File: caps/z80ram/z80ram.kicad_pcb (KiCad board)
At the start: 4 copper layers, 85 x 56 mm, 19 parts, among them J10 PORTG, J2 PORTA, J3 PORTB, J5 PORTD, J6 PORTE, J7 PORTF, U1 74HCT257, U2 AS6C4008-55PCN, U3 74HCT574, U4 Z80CPU

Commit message: OCD tweaks
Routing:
- net /PA6: track 90.7 -> 87.6 mm
- net /PD2: track 69.2 -> 66.7 mm
- net /PD6: track 62.3 -> 60.9 mm
- net /PD4: track 65.3 -> 64.1 mm
- net /PE2: track 131.9 -> 133.1 mm
- net /PB1: track 35.1 -> 36.0 mm
- net /PE0: track 111.4 -> 112.0 mm
- net /PD5: track 57.9 -> 57.2 mm
- net GND: vias 81 -> 82

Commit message: Final (?!) tweaks
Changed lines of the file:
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@@
 	)
 	(segment
-		(start 182.481637 110.043082)
-		(end 182.481637 109.15472)
+		(start 182.25 110.274719)
+		(end 182.25 109.386357)
 		(width 0.25)
 		(layer "F.Cu")
@@
 	(segment
 		(start 182.003241 110.521478)
-		(end 182.481637 110.043082)
+		(end 182.25 110.274719)
 		(width 0.25)
 		(layer "F.Cu")
@@
 	)
 	(segment
-		(start 182.481637 109.15472)
+		(start 182.25 109.386357)
 		(end 184.092757 107.5436)
 		(width 0.25)

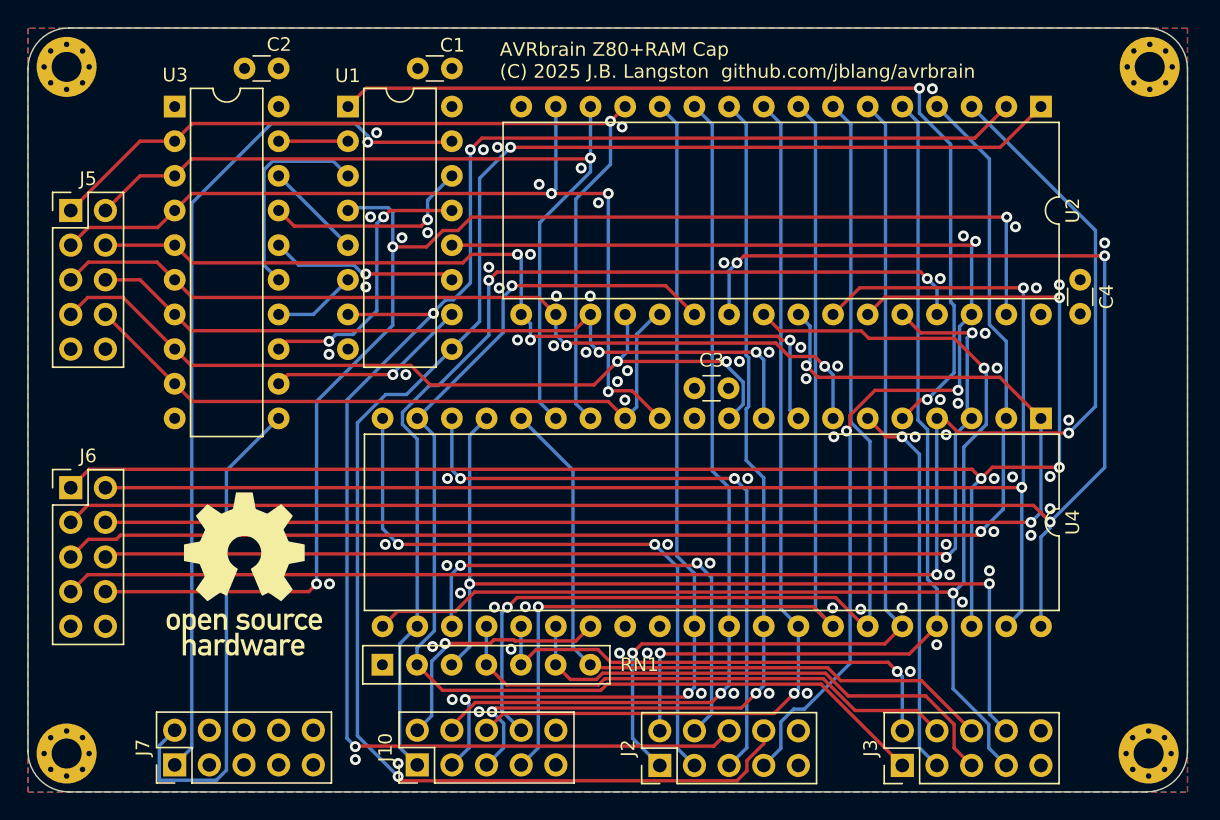
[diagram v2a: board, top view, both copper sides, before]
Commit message: Add reset and halt buttons to Z80 cap
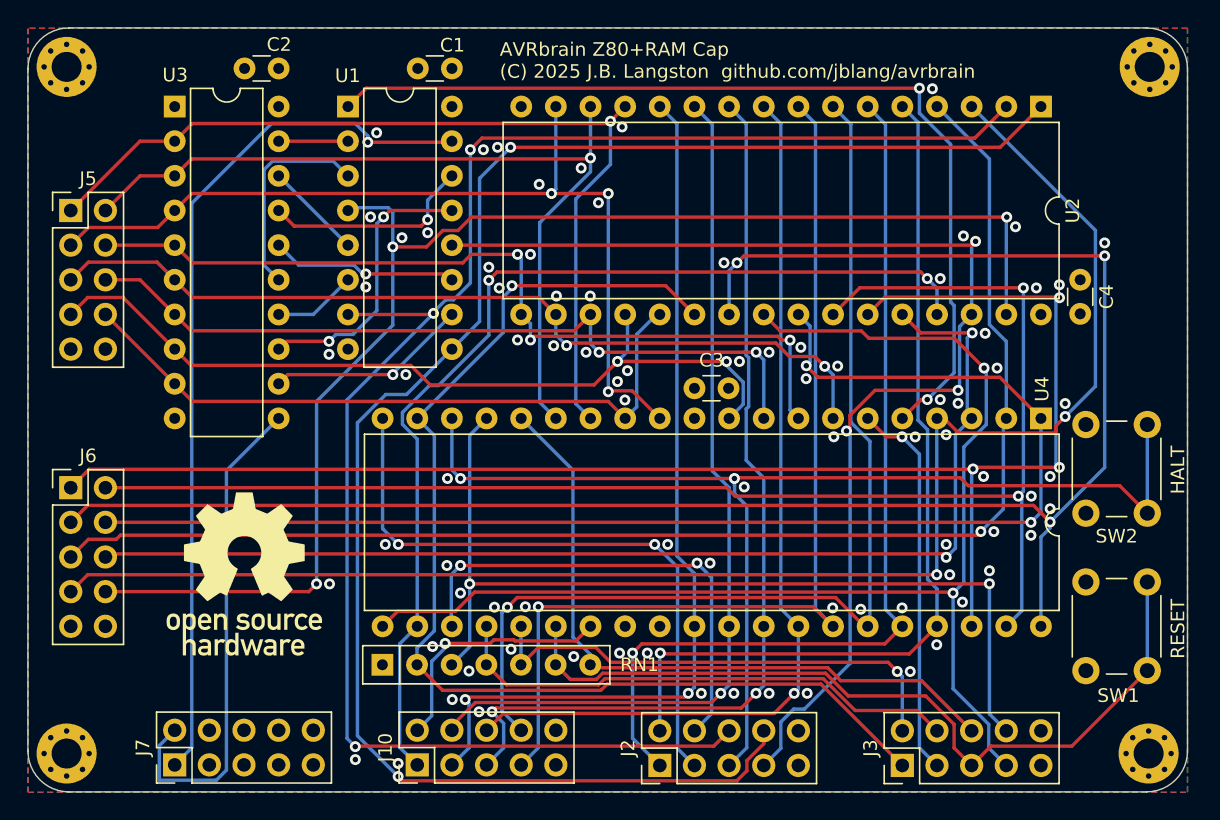
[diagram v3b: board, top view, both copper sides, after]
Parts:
- added SW1: RESET, Button_Switch_THT:SW_PUSH_6mm, F.Cu at (199.6, 128.1)
- added SW2: HALT, Button_Switch_THT:SW_PUSH_6mm, F.Cu at (199.6, 116.5)
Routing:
- net /PA4: track 46.7 -> 84.6 mm
- net /PB4: track 37.8 -> 60.0 mm
- net /PE6: track 114.1 -> 113.5 mm
- net GND: vias 82 -> 84
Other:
- board text added: "HALT"
- board text added: "RESET"
